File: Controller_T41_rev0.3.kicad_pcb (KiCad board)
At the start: 2 copper layers, 102.9 x 69.9 mm, 54 parts, among them J1 8P8C_x4, J2 8P8C_x4, J3 Screw_Terminal_01x02, J4 RJ45_LED, U1 Teensy4.1, U2 AMS1117-5.0, U3 74HCT245, U4 74HCT245, U5 74HCT245, U6 74HCT245

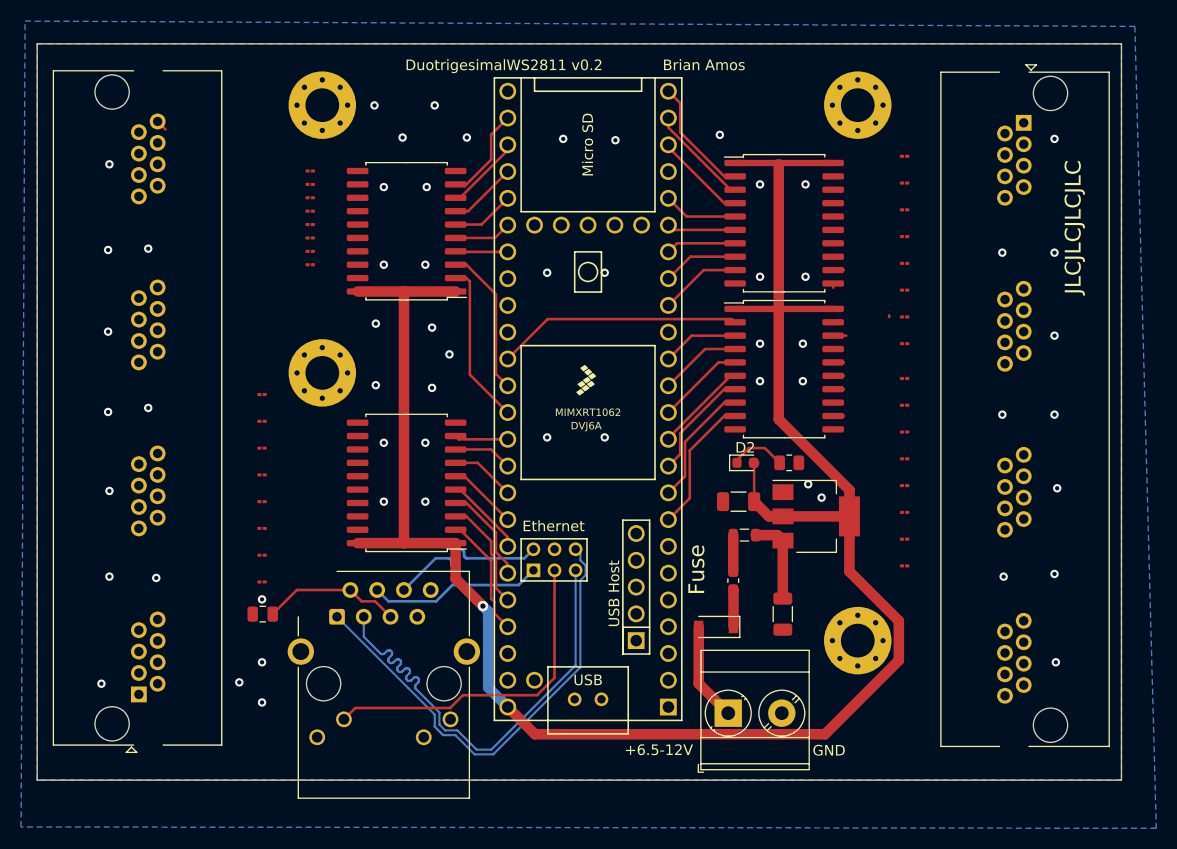
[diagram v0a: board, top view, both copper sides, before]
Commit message: Smaller resistors, larger fuse, additional labeling on silkscreen
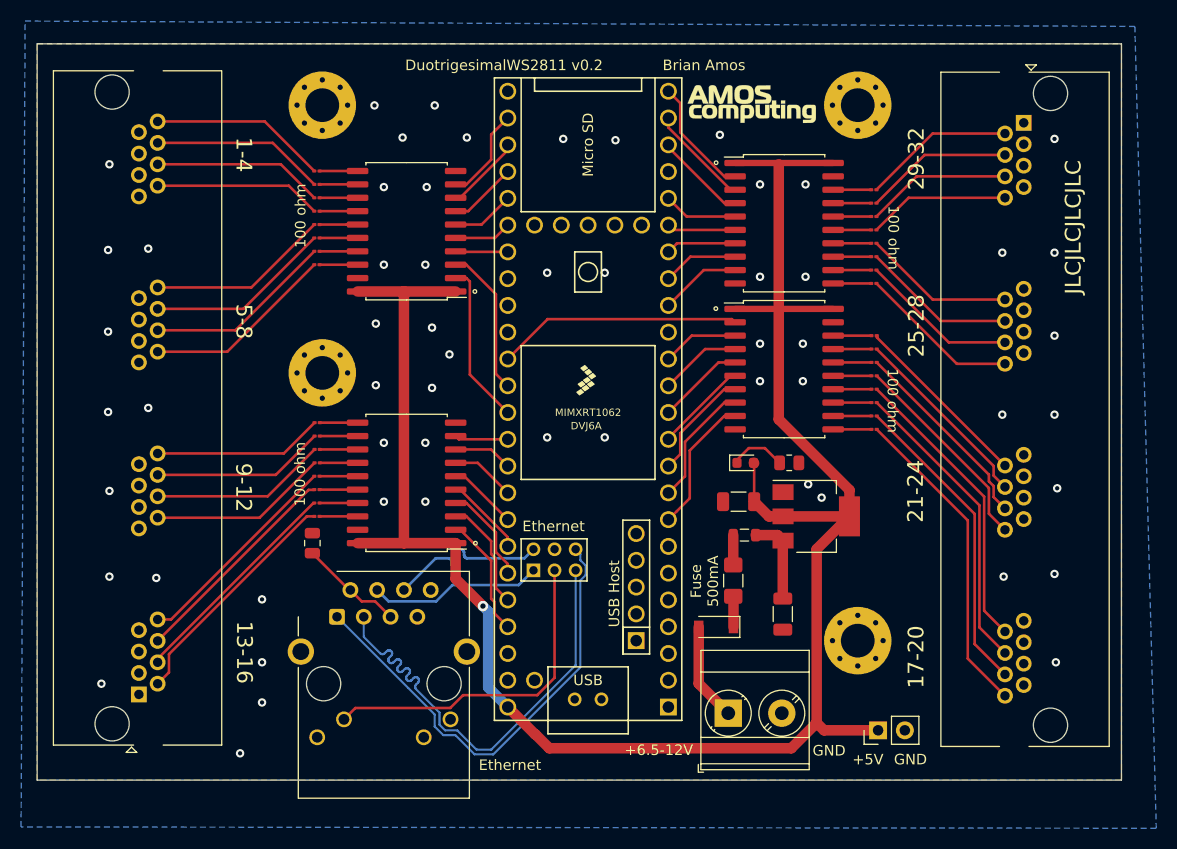
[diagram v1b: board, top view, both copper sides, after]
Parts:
- added G***: LOGO, Controller_T41_rev0.2:logo, F.Cu at (164.4, 56.5)
- added J5: 5v Conn, Connector_PinHeader_2.54mm:PinHeader_1x02_P2.54mm_Vertical, F.Cu at (176.3, 115.9)
- F1: footprint Fuse:Fuse_0603_1608Metric_Pad1.05x0.95mm_HandSolder -> Fuse:Fuse_1206_3216Metric_Pad1.42x1.75mm_HandSolder
- moved R9 13.3 mm to (175.9, 87.4)
- moved R8 12.0 mm to (175.9, 86.1)
- moved R7 10.8 mm to (175.9, 84.8)
- moved R6 9.59 mm to (175.9, 83.6)
- moved R5 8.39 mm to (175.9, 82.3)
- moved C3 8.21 mm to (122.6, 98.2), turned to 270 degrees
- moved R26 8.11 mm to (123.1, 95.6)
- moved R4 7.21 mm to (175.9, 81.0)
- moved R27 7.19 mm to (123.1, 94.4)
- moved R25 6.42 mm to (175.9, 73.5)
- moved R28 6.38 mm to (123.1, 93.1)
- moved R3 6.07 mm to (175.9, 79.8)
- moved R33 5.87 mm to (123.1, 86.7)
- moved R29 5.74 mm to (123.1, 91.8)
- moved R32 5.42 mm to (123.1, 88.0)
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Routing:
- net L_08: track 0.44 -> 30.7 mm
- net L_07: track 0.00 -> 29.5 mm
- net L_06: track 0.00 -> 28.8 mm
- net L_05: track 0.00 -> 28.0 mm
- net L_31: track 0.00 -> 22.4 mm
- net L_32: track 0.00 -> 21.3 mm
- net L_33: track 0.00 -> 20.8 mm
- net L_34: track 0.00 -> 20.5 mm
- net L_04: track 0.63 -> 20.2 mm
- net L_03: track 0.00 -> 18.9 mm
- net L_21: track 0.00 -> 18.2 mm
- net L_02: track 0.31 -> 18.4 mm
- net L_22: track 0.00 -> 17.9 mm
- net L_23: track 0.00 -> 17.6 mm
- net L_01: track 0.20 -> 17.5 mm
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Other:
- board text added: "+5V"
- board text added: "1-4"
- board text added: "100 ohm"
- board text added: "13-16"
- board text added: "17-20"
- board text added: "21-24"
- board text added: "25-28"
- board text added: "5-8"
- board text added: "9-12"
- board text added: "Ethernet"
- board text added: "Fuse 500mA"
- board text removed: "Fuse"

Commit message: Minor Placement Updates
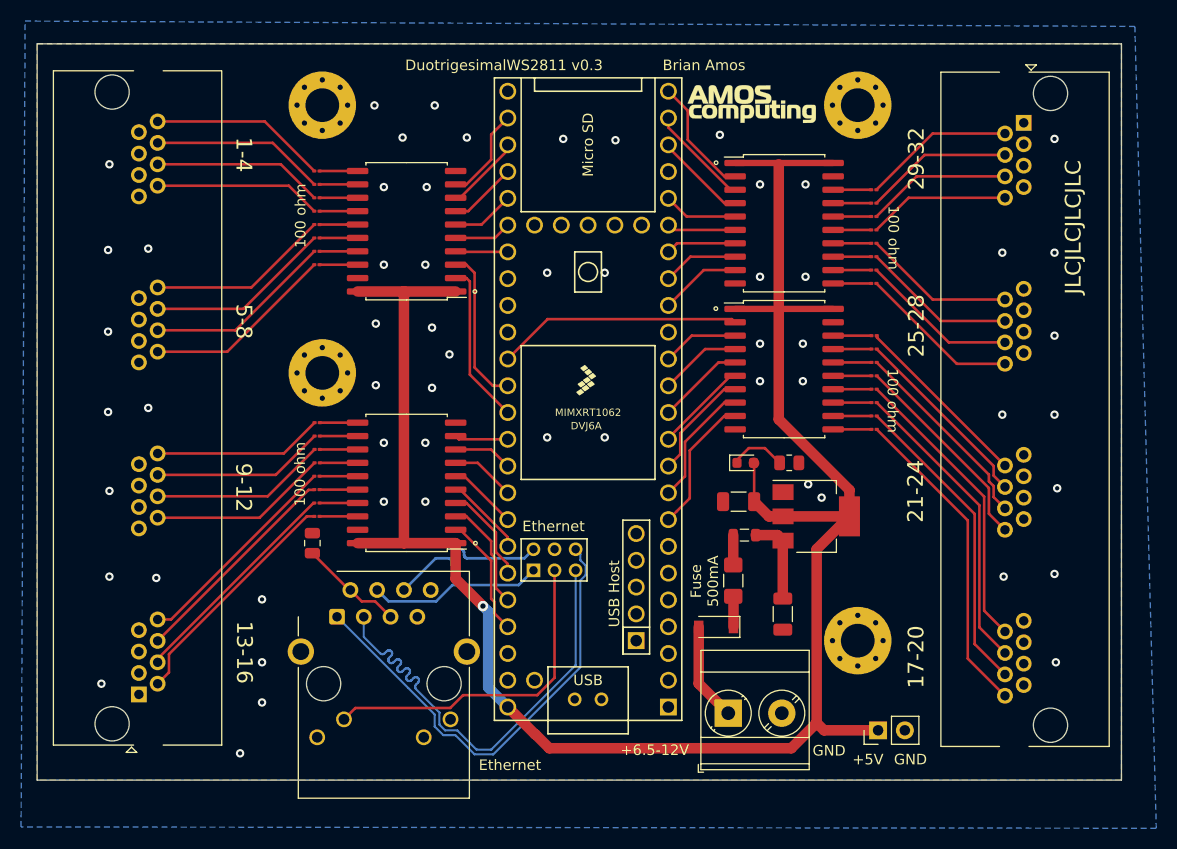
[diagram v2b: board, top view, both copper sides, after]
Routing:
- net P_23: track 14.1 -> 15.0 mm
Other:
- board text added: "DuotrigesimalWS2811 v0.3 Brian Amos"
- board text removed: "DuotrigesimalWS2811 v0.2 Brian Amos"
